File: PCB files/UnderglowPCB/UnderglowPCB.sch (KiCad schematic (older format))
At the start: 71 parts, among them J1 Conn_01x03, J10 Conn_01x03, J11 Conn_01x05, J12 Conn_01x07, J2 DB9_Male, J3 USB_B_Micro, J4 Conn_01x03, J5 Conn_01x03, J6 Conn_01x03, J7 Conn_01x03, J8 Conn_01x03, J9 Conn_01x03, Q1 S8050, Q2 S8050, U1 ESP32-WROOM-32D, U2 LMR14030-Q1, U3 NCP1117-3.3_SOT223, U4 TXB0108DQSR, U6 SN65HVD230, U7 USBLC6-2SC6, U8 CP2102N-A01-GQFN28

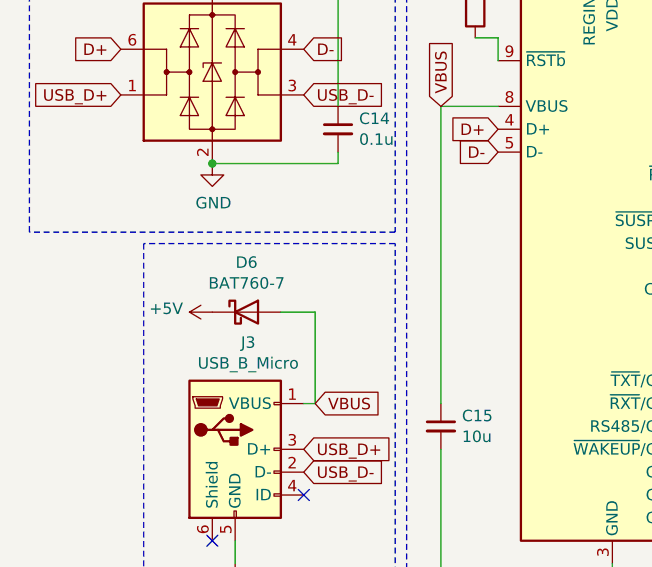
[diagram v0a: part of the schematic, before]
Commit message: PCB data updated, 1.3.2 ordering information is provided.
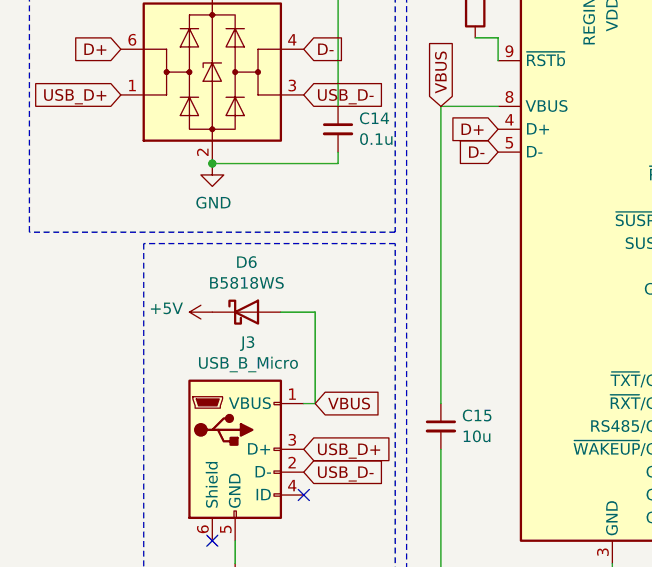
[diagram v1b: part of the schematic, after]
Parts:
- D3: footprint UnderglowPCB:TPSMA6L15A -> UnderglowPCB:DO-221AC
- D6: value BAT760-7 -> B5818WS
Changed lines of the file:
@@
 Title "Open Underglow Controller"
 Date "2021-04-06"
-Rev "1.3.0"
+Rev "1.3.2"
 Comp "Jeremy Stintzcum"
 Comment1 ""
@@
 P 1500 2300
 F 0 "D6" H 1500 2517 50  0000 C CNN
-F 1 "BAT760-7" H 1500 2426 50  0000 C CNN
+F 1 "B5818WS" H 1500 2426 50  0000 C CNN
 F 2 "Diode_SMD:D_SOD-323" H 1500 2300 50  0001 C CNN
 F 3 "~" H 1500 2300 50  0001 C CNN
@@
 F 0 "D3" V 5300 7250 50  0000 L CNN
 F 1 "VSSAF512" V 5400 7050 50  0000 L CNN
-F 2 "UnderglowPCB:TPSMA6L15A" V 5150 7350 50  0001 C CNN
+F 2 "UnderglowPCB:DO-221AC" V 5150 7350 50  0001 C CNN
 F 3 "~" V 5150 7350 50  0001 C CNN
 	1    5150 7350
